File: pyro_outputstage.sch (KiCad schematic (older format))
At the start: 7 parts, among them Q302 BC847BDW1, U301 SI7232DN

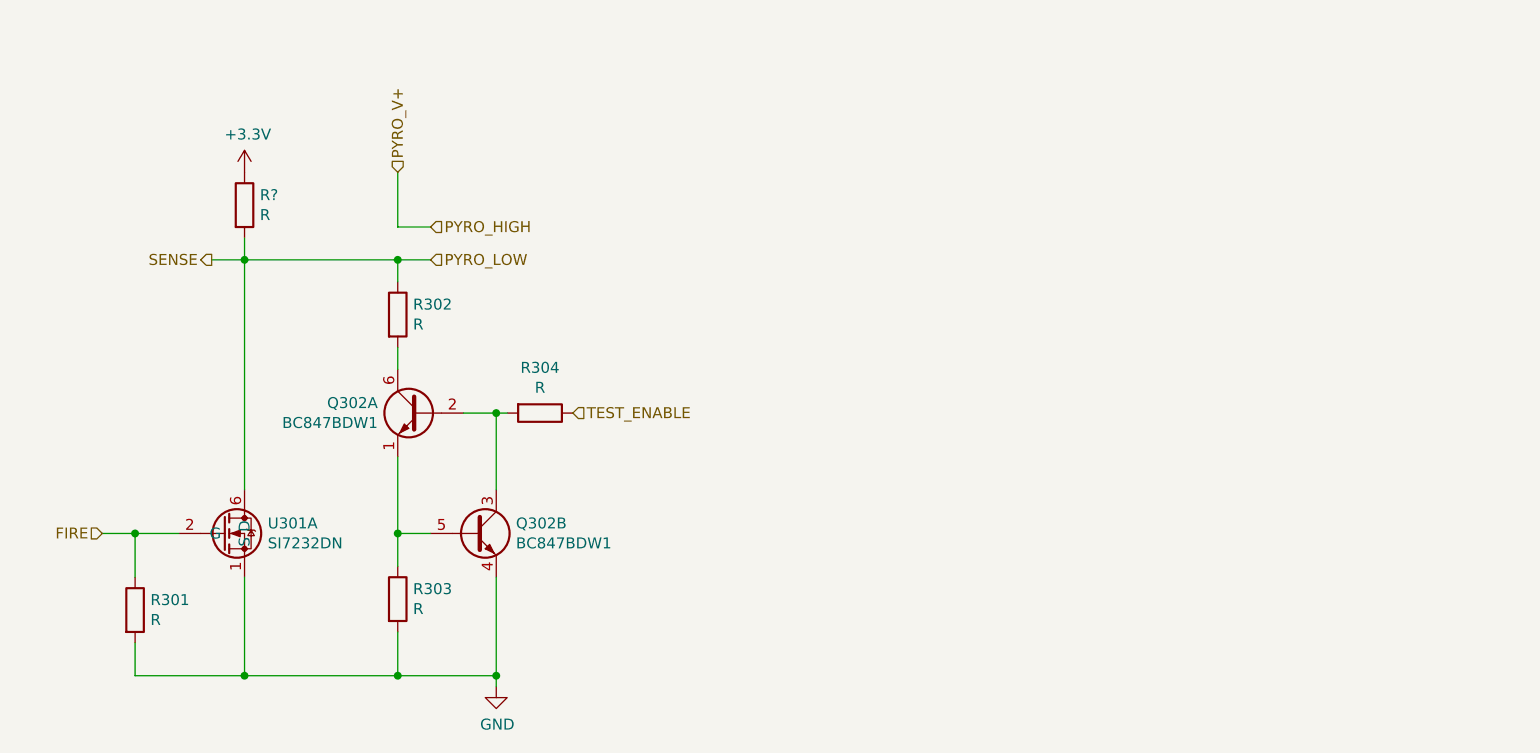
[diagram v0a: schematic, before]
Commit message: update pyro output stage. add a fuse to the test circuit and remove pullup for sense line
Signed-off-by: Thomas Schmid <tom@binary-kitchen.de>
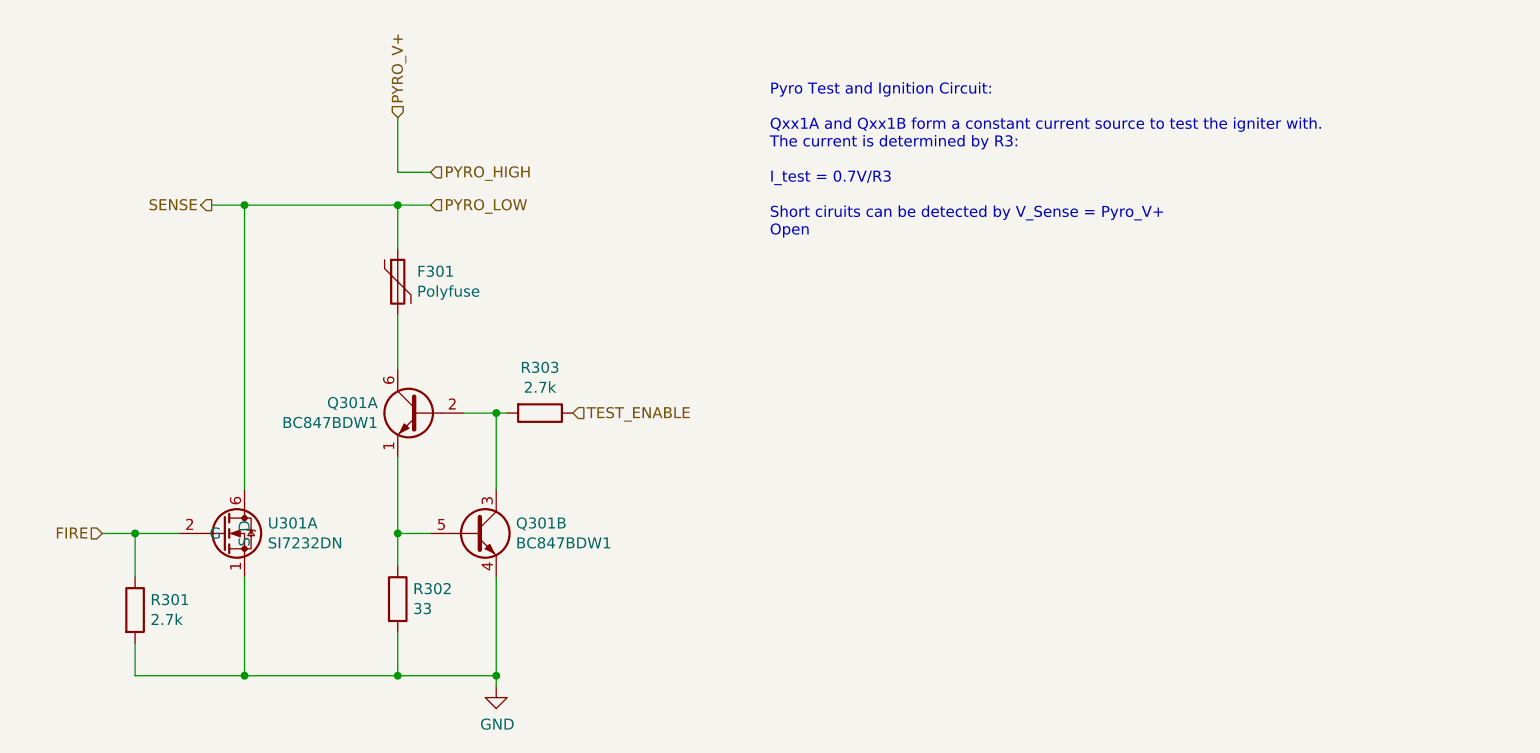
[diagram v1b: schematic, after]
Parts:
- removed R302, R?: R, Resistor_SMD:R_0603_1608Metric_Pad1.05x0.95mm_HandSolder, symbol Device:R
- added F301: Polyfuse, Fuse:Fuse_0603_1608Metric_Pad1.05x0.95mm_HandSolder, symbol Device:Polyfuse
- R301: value R -> 2.7k; footprint Resistor_SMD:R_0603_1608Metric_Pad1.05x0.95mm_HandSolder -> Resistor_SMD:R_0402_1005Metric
- R302: renamed from R303; value R -> 33; footprint Resistor_SMD:R_0603_1608Metric_Pad1.05x0.95mm_HandSolder -> Resistor_SMD:R_0402_1005Metric
- R303: renamed from R304; value R -> 2.7k; footprint Resistor_SMD:R_0603_1608Metric_Pad1.05x0.95mm_HandSolder -> Resistor_SMD:R_0402_1005Metric
- renumbered Q302 to Q301
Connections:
- net PYRO_LOW: now also F301.1
- net at Q301.6 (C1): now also F301.2
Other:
- note added: "Pyro Test and Ignition Circuit:\n\nQxx1A and Qxx1B form a constant current source to test the igniter with.\nThe current is determined by R3:\n\nI_test = 0.7V/R3\n\nShort ciruits can be detected by V_Sense = Pyro_V+\nOpen"
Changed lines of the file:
@@
 P 5850 4350
 AR Path="/5D4757F5" Ref="R?"  Part="1"
-AR Path="/5D473C9B/5D4757F5" Ref="R303"  Part="1"
+AR Path="/5D473C9B/5D4757F5" Ref="R302"  Part="1"
 AR Path="/5D47A891/5D4757F5" Ref="R?"  Part="1"
 AR Path="/5D47CE84/5D4757F5" Ref="R?"  Part="1"
-AR Path="/5D488E46/5D4757F5" Ref="R403"  Part="1"
-AR Path="/5D48B429/5D4757F5" Ref="R503"  Part="1"
-F 0 "R303" H 5920 4396 50  0000 L CNN
-F 1 "R" H 5920 4305 50  0000 L CNN
-F 2 "Resistor_SMD:R_0603_1608Metric_Pad1.05x0.95mm_HandSolder" V 5780 4350 50  0001 C CNN
+AR Path="/5D488E46/5D4757F5" Ref="R402"  Part="1"
+AR Path="/5D48B429/5D4757F5" Ref="R502"  Part="1"
+F 0 "R302" H 5920 4396 50  0000 L CNN
+F 1 "33" H 5920 4305 50  0000 L CNN
+F 2 "Resistor_SMD:R_0402_1005Metric" V 5780 4350 50  0001 C CNN
 F 3 "~" H 5850 4350 50  0001 C CNN
 	1    5850 4350
@@
 P 6300 4750
 AR Path="/5D475801" Ref="#PWR?"  Part="1"
-AR Path="/5D473C9B/5D475801" Ref="#PWR0136"  Part="1"
+AR Path="/5D473C9B/5D475801" Ref="#PWR0301"  Part="1"
 AR Path="/5D47A891/5D475801" Ref="#PWR?"  Part="1"
 AR Path="/5D47CE84/5D475801" Ref="#PWR?"  Part="1"
-AR Path="/5D488E46/5D475801" Ref="#PWR0137"  Part="1"
-AR Path="/5D48B429/5D475801" Ref="#PWR0138"  Part="1"
-F 0 "#PWR0136" H 6300 4500 50  0001 C CNN
+AR Path="/5D488E46/5D475801" Ref="#PWR0401"  Part="1"
+AR Path="/5D48B429/5D475801" Ref="#PWR0501"  Part="1"
+F 0 "#PWR0301" H 6300 4500 50  0001 C CNN
 F 1 "GND" H 6305 4577 50  0000 C CNN
 F 2 "" H 6300 4750 50  0001 C CNN
@@
 P 6500 3500
 AR Path="/5D47580C" Ref="R?"  Part="1"
-AR Path="/5D473C9B/5D47580C" Ref="R304"  Part="1"
+AR Path="/5D473C9B/5D47580C" Ref="R303"  Part="1"
 AR Path="/5D47A891/5D47580C" Ref="R?"  Part="1"
 AR Path="/5D47CE84/5D47580C" Ref="R?"  Part="1"
-AR Path="/5D488E46/5D47580C" Ref="R404"  Part="1"
-AR Path="/5D48B429/5D47580C" Ref="R504"  Part="1"
-F 0 "R304" V 6293 3500 50  0000 C CNN
-F 1 "R" V 6384 3500 50  0000 C CNN
-F 2 "Resistor_SMD:R_0603_1608Metric_Pad1.05x0.95mm_HandSolder" V 6430 3500 50  0001 C CNN
+AR Path="/5D488E46/5D47580C" Ref="R403"  Part="1"
+AR Path="/5D48B429/5D47580C" Ref="R503"  Part="1"
+F 0 "R303" V 6293 3500 50  0000 C CNN
+F 1 "2.7k" V 6384 3500 50  0000 C CNN
+F 2 "Resistor_SMD:R_0402_1005Metric" V 6430 3500 50  0001 C CNN
 F 3 "~" H 6500 3500 50  0001 C CNN
 	1    6500 3500
@@
 	6300 3500 6350 3500
 Connection ~ 6300 3500
-$Comp
-L Device:R R?
-U 1 1 5D475815
-P 5850 3050
-AR Path="/5D475815" Ref="R?"  Part="1"
-AR Path="/5D473C9B/5D475815" Ref="R302"  Part="1"
-AR Path="/5D47A891/5D475815" Ref="R?"  Part="1"
-AR Path="/5D47CE84/5D475815" Ref="R?"  Part="1"
-AR Path="/5D488E46/5D475815" Ref="R402"  Part="1"
-AR Path="/5D48B429/5D475815" Ref="R502"  Part="1"
-F 0 "R302" H 5920 3096 50  0000 L CNN
-F 1 "R" H 5920 3005 50  0000 L CNN
-F 2 "Resistor_SMD:R_0603_1608Metric_Pad1.05x0.95mm_HandSolder" V 5780 3050 50  0001 C CNN
-F 3 "~" H 5850 3050 50  0001 C CNN
-	1    5850 3050
-	1    0    0    -1
-$EndComp
-Wire Wire Line
-	5850 3200 5850 3300
-Wire Wire Line
-	6000 2800 5850 2800
-Wire Wire Line
-	5850 2800 5850 2900
-Wire Wire Line
-	6000 2650 5850 2650
-Wire Wire Line
-	5850 2650 5850 2400
-Wire Wire Line
-	5850 2800 5150 2800
-Wire Wire Line
-	5150 2800 5150 3850
-Connection ~ 5850 2800
+Wire Wire Line
+	6000 2400 5850 2400
+Wire Wire Line
+	5850 2400 5850 2150
 Wire Wire Line
 	5850 4700 5150 4700
@@
 AR Path="/5D48B429/5D475828" Ref="R501"  Part="1"
 F 0 "R301" H 4720 4446 50  0000 L CNN
-F 1 "R" H 4720 4355 50  0000 L CNN
-F 2 "Resistor_SMD:R_0603_1608Metric_Pad1.05x0.95mm_HandSolder" V 4580 4400 50  0001 C CNN
+F 1 "2.7k" H 4720 4355 50  0000 L CNN
+F 2 "Resistor_SMD:R_0402_1005Metric" V 4580 4400 50  0001 C CNN
 F 3 "~" H 4650 4400 50  0001 C CNN
 	1    4650 4400
@@
 P 5950 3500
 AR Path="/5D475835" Ref="Q?"  Part="1"
-AR Path="/5D473C9B/5D475835" Ref="Q302"  Part="1"
+AR Path="/5D473C9B/5D475835" Ref="Q301"  Part="1"
 AR Path="/5D47A891/5D475835" Ref="Q?"  Part="1"
 AR Path="/5D47CE84/5D475835" Ref="Q?"  Part="1"
-AR Path="/5D488E46/5D475835" Ref="Q402"  Part="1"
-AR Path="/5D48B429/5D475835" Ref="Q502"  Part="1"
-F 0 "Q302" H 6141 3546 50  0000 L CNN
+AR Path="/5D488E46/5D475835" Ref="Q401"  Part="1"
+AR Path="/5D48B429/5D475835" Ref="Q501"  Part="1"
+F 0 "Q301" H 6141 3546 50  0000 L CNN
 F 1 "BC847BDW1" H 6141 3455 50  0000 L CNN
 F 2 "Package_TO_SOT_SMD:SOT-363_SC-70-6" H 6150 3600 50  0001 C CNN
@@
 P 6200 4050
 AR Path="/5D47583B" Ref="Q?"  Part="2"
-AR Path="/5D473C9B/5D47583B" Ref="Q302"  Part="2"
+AR Path="/5D473C9B/5D47583B" Ref="Q301"  Part="2"
 AR Path="/5D47A891/5D47583B" Ref="Q?"  Part="2"
 AR Path="/5D47CE84/5D47583B" Ref="Q?"  Part="2"
-AR Path="/5D488E46/5D47583B" Ref="Q402"  Part="2"
-AR Path="/5D48B429/5D47583B" Ref="Q502"  Part="2"
-F 0 "Q302" H 6390 4096 50  0000 L CNN
+AR Path="/5D488E46/5D47583B" Ref="Q401"  Part="2"
+AR Path="/5D48B429/5D47583B" Ref="Q501"  Part="2"
+F 0 "Q301" H 6390 4096 50  0000 L CNN
 F 1 "BC847BDW1" H 6390 4005 50  0000 L CNN
 F 2 "Package_TO_SOT_SMD:SOT-363_SC-70-6" H 6400 4150 50  0001 C CNN
@@
 Text HLabel 6650 3500 2    50   Input ~ 0
 TEST_ENABLE
-Text HLabel 6000 2800 2    50   Input ~ 0
+Text HLabel 6000 2550 2    50   Input ~ 0
 PYRO_LOW
-Text HLabel 6000 2650 2    50   Input ~ 0
+Text HLabel 6000 2400 2    50   Input ~ 0
 PYRO_HIGH
-Text HLabel 5850 2400 1    50   Input ~ 0
+Text HLabel 5850 2150 1    50   Input ~ 0
 PYRO_V+
 Text HLabel 4500 4050 0    50   Input ~ 0
 FIRE
-Text HLabel 5000 2800 0    50   Output ~ 0
+Text HLabel 5000 2550 0    50   Output ~ 0
 SENSE
-Wire Wire Line
-	5000 2800 5150 2800
-Connection ~ 5150 2800
 $Comp
 L altimeter:SI7232DN U301
@@
 	1    0    0    -1
 $EndComp
-$Comp
-L Device:R R?
-U 1 1 5D503484
-P 5150 2550
-AR Path="/5D503484" Ref="R?"  Part="1"
-AR Path="/5D473C9B/5D503484" Ref="R?"  Part="1"
-AR Path="/5D47A891/5D503484" Ref="R?"  Part="1"
-AR Path="/5D47CE84/5D503484" Ref="R?"  Part="1"
-AR Path="/5D488E46/5D503484" Ref="R?"  Part="1"
-AR Path="/5D48B429/5D503484" Ref="R?"  Part="1"
-F 0 "R?" H 5220 2596 50  0000 L CNN
-F 1 "R" H 5220 2505 50  0000 L CNN
-F 2 "Resistor_SMD:R_0603_1608Metric_Pad1.05x0.95mm_HandSolder" V 5080 2550 50  0001 C CNN
-F 3 "~" H 5150 2550 50  0001 C CNN
-	1    5150 2550
-	1    0    0    -1
-$EndComp
-Wire Wire Line
-	5150 2700 5150 2800
-$Comp
-L power:+3.3V #PWR?
-U 1 1 5D50478E
-P 5150 2400
-AR Path="/5D488E46/5D50478E" Ref="#PWR?"  Part="1"
-AR Path="/5D473C9B/5D50478E" Ref="#PWR?"  Part="1"
-F 0 "#PWR?" H 5150 2250 50  0001 C CNN
-F 1 "+3.3V" H 5165 2573 50  0000 C CNN
-F 2 "" H 5150 2400 50  0001 C CNN
-F 3 "" H 5150 2400 50  0001 C CNN
-	1    5150 2400
-	1    0    0    -1
-$EndComp
+Text Notes 7550 2700 0    50   ~ 0
+Pyro Test and Ignition Circuit:\n\nQxx1A and Qxx1B form a constant current source to test the igniter with.\nThe current is determined by R3:\n\nI_test = 0.7V/R3\n\nShort ciruits can be detected by V_Sense = Pyro_V+\nOpen
+Wire Wire Line
+	5000 2550 5150 2550
+Connection ~ 5850 2550
+Wire Wire Line
+	5850 2550 6000 2550
+Connection ~ 5150 2550
+Wire Wire Line
+	5150 2550 5850 2550
+$Comp
+L Device:Polyfuse F301
+U 1 1 5D6F3FF8
+P 5850 2900
+AR Path="/5D473C9B/5D6F3FF8" Ref="F301"  Part="1"
+AR Path="/5D488E46/5D6F3FF8" Ref="F401"  Part="1"
+AR Path="/5D48B429/5D6F3FF8" Ref="F501"  Part="1"
+F 0 "F301" H 5938 2946 50  0000 L CNN
+F 1 "Polyfuse" H 5938 2855 50  0000 L CNN
+F 2 "Fuse:Fuse_0603_1608Metric_Pad1.05x0.95mm_HandSolder" H 5900 2700 50  0001 L CNN
+F 3 "~" H 5850 2900 50  0001 C CNN
+	1    5850 2900
+	1    0    0    -1
+$EndComp
+Wire Wire Line
+	5150 2550 5150 3850
+Wire Wire Line
+	5850 2750 5850 2550
+Wire Wire Line
+	5850 3050 5850 3300
 $EndSCHEMATC

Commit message: more work on schematic and layout
Signed-off-by: Thomas Schmid <tom@lfence.de>
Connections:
- net FIRE: now also U301.4 (G); no longer U301.2 (G)
- net GND: now also U301.3 (S); no longer U301.1 (S)
- net PYRO_LOW: now also U301.5 (D); no longer U301.6 (D)
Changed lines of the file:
@@
 AR Path="/5D488E46/5D475801" Ref="#PWR0401"  Part="1"
 AR Path="/5D48B429/5D475801" Ref="#PWR0501"  Part="1"
-F 0 "#PWR0301" H 6300 4500 50  0001 C CNN
+F 0 "#PWR0501" H 6300 4500 50  0001 C CNN
 F 1 "GND" H 6305 4577 50  0000 C CNN
 F 2 "" H 6300 4750 50  0001 C CNN
@@
 $Comp
 L altimeter:SI7232DN U301
-U 1 1 5D4F79DE
+U 2 1 5D4F79DE
 P 5150 4050
-AR Path="/5D473C9B/5D4F79DE" Ref="U301"  Part="1"
-AR Path="/5D488E46/5D4F79DE" Ref="U301"  Part="2"
+AR Path="/5D473C9B/5D4F79DE" Ref="U301"  Part="2"
+AR Path="/5D488E46/5D4F79DE" Ref="U301"  Part="1"
 AR Path="/5D48B429/5D4F79DE" Ref="U501"  Part="1"
 F 0 "U301" H 5256 4096 50  0000 L CNN
@@
 F 2 "Package_SO:Vishay_PowerPAK_1212-8_Dual" H 5150 4050 50  0001 C CNN
 F 3 "" H 5150 4050 50  0001 C CNN
-	1    5150 4050
+	2    5150 4050
 	1    0    0    -1
 $EndComp

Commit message: update
Signed-off-by: Thomas Schmid <tom@lfence.de>
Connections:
- net FIRE: now also U301.2 (G); no longer U301.4 (G)
- net GND: now also U301.1 (S); no longer U301.3 (S)
- net PYRO_LOW: now also U301.6 (D); no longer U301.5 (D)
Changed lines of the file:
@@
 $Descr A4 11693 8268
 encoding utf-8
-Sheet 3 5
+Sheet 5 5
 Title ""
 Date ""
@@
 AR Path="/5D488E46/5D4757F5" Ref="R402"  Part="1"
 AR Path="/5D48B429/5D4757F5" Ref="R502"  Part="1"
-F 0 "R302" H 5920 4396 50  0000 L CNN
+F 0 "R502" H 5920 4396 50  0000 L CNN
 F 1 "33" H 5920 4305 50  0000 L CNN
 F 2 "Resistor_SMD:R_0402_1005Metric" V 5780 4350 50  0001 C CNN
@@
 AR Path="/5D488E46/5D47580C" Ref="R403"  Part="1"
 AR Path="/5D48B429/5D47580C" Ref="R503"  Part="1"
-F 0 "R303" V 6293 3500 50  0000 C CNN
+F 0 "R503" V 6293 3500 50  0000 C CNN
 F 1 "2.7k" V 6384 3500 50  0000 C CNN
 F 2 "Resistor_SMD:R_0402_1005Metric" V 6430 3500 50  0001 C CNN
@@
 AR Path="/5D488E46/5D475828" Ref="R401"  Part="1"
 AR Path="/5D48B429/5D475828" Ref="R501"  Part="1"
-F 0 "R301" H 4720 4446 50  0000 L CNN
+F 0 "R501" H 4720 4446 50  0000 L CNN
 F 1 "2.7k" H 4720 4355 50  0000 L CNN
 F 2 "Resistor_SMD:R_0402_1005Metric" V 4580 4400 50  0001 C CNN
@@
 AR Path="/5D488E46/5D475835" Ref="Q401"  Part="1"
 AR Path="/5D48B429/5D475835" Ref="Q501"  Part="1"
-F 0 "Q301" H 6141 3546 50  0000 L CNN
+F 0 "Q501" H 6141 3546 50  0000 L CNN
 F 1 "BC847BDW1" H 6141 3455 50  0000 L CNN
 F 2 "Package_TO_SOT_SMD:SOT-363_SC-70-6" H 6150 3600 50  0001 C CNN
@@
 AR Path="/5D488E46/5D47583B" Ref="Q401"  Part="2"
 AR Path="/5D48B429/5D47583B" Ref="Q501"  Part="2"
-F 0 "Q301" H 6390 4096 50  0000 L CNN
+F 0 "Q501" H 6390 4096 50  0000 L CNN
 F 1 "BC847BDW1" H 6390 4005 50  0000 L CNN
 F 2 "Package_TO_SOT_SMD:SOT-363_SC-70-6" H 6400 4150 50  0001 C CNN
@@
 $Comp
 L altimeter:SI7232DN U301
-U 2 1 5D4F79DE
+U 1 1 5D4F79DE
 P 5150 4050
 AR Path="/5D473C9B/5D4F79DE" Ref="U301"  Part="2"
 AR Path="/5D488E46/5D4F79DE" Ref="U301"  Part="1"
 AR Path="/5D48B429/5D4F79DE" Ref="U501"  Part="1"
-F 0 "U301" H 5256 4096 50  0000 L CNN
+F 0 "U501" H 5256 4096 50  0000 L CNN
 F 1 "SI7232DN" H 5256 4005 50  0000 L CNN
 F 2 "Package_SO:Vishay_PowerPAK_1212-8_Dual" H 5150 4050 50  0001 C CNN
 F 3 "" H 5150 4050 50  0001 C CNN
-	2    5150 4050
+	1    5150 4050
 	1    0    0    -1
 $EndComp
@@
 AR Path="/5D488E46/5D6F3FF8" Ref="F401"  Part="1"
 AR Path="/5D48B429/5D6F3FF8" Ref="F501"  Part="1"
-F 0 "F301" H 5938 2946 50  0000 L CNN
+F 0 "F501" H 5938 2946 50  0000 L CNN
 F 1 "Polyfuse" H 5938 2855 50  0000 L CNN
 F 2 "Fuse:Fuse_0603_1608Metric_Pad1.05x0.95mm_HandSolder" H 5900 2700 50  0001 L CNN

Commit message: update to schematic and layout
Signed-off-by: Thomas Schmid <tom@lfence.de>
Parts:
- added R3: 68k, Resistor_SMD:R_0402_1005Metric, symbol Device:R
- added R4: 220k, Resistor_SMD:R_0402_1005Metric, symbol Device:R
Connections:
- net GND: now also R3.2
- net PYRO_LOW: now also R4.1
- new net SENSE: R3.1, R4.2
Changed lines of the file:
@@
 $Descr A4 11693 8268
 encoding utf-8
-Sheet 5 5
+Sheet 6 6
 Title ""
 Date ""
@@
 AR Path="/5D488E46/5D4757F5" Ref="R402"  Part="1"
 AR Path="/5D48B429/5D4757F5" Ref="R502"  Part="1"
-F 0 "R502" H 5920 4396 50  0000 L CNN
+AR Path="/5D4E7D5B/5D4757F5" Ref="R12"  Part="1"
+F 0 "R12" H 5920 4396 50  0000 L CNN
 F 1 "33" H 5920 4305 50  0000 L CNN
 F 2 "Resistor_SMD:R_0402_1005Metric" V 5780 4350 50  0001 C CNN
@@
 AR Path="/5D488E46/5D475801" Ref="#PWR0401"  Part="1"
 AR Path="/5D48B429/5D475801" Ref="#PWR0501"  Part="1"
-F 0 "#PWR0501" H 6300 4500 50  0001 C CNN
+AR Path="/5D4E7D5B/5D475801" Ref="#PWR0136"  Part="1"
+F 0 "#PWR0136" H 6300 4500 50  0001 C CNN
 F 1 "GND" H 6305 4577 50  0000 C CNN
 F 2 "" H 6300 4750 50  0001 C CNN
@@
 AR Path="/5D488E46/5D47580C" Ref="R403"  Part="1"
 AR Path="/5D48B429/5D47580C" Ref="R503"  Part="1"
-F 0 "R503" V 6293 3500 50  0000 C CNN
+AR Path="/5D4E7D5B/5D47580C" Ref="R13"  Part="1"
+F 0 "R13" V 6293 3500 50  0000 C CNN
 F 1 "2.7k" V 6384 3500 50  0000 C CNN
 F 2 "Resistor_SMD:R_0402_1005Metric" V 6430 3500 50  0001 C CNN
@@
 AR Path="/5D488E46/5D475828" Ref="R401"  Part="1"
 AR Path="/5D48B429/5D475828" Ref="R501"  Part="1"
-F 0 "R501" H 4720 4446 50  0000 L CNN
+AR Path="/5D4E7D5B/5D475828" Ref="R10"  Part="1"
+F 0 "R10" H 4720 4446 50  0000 L CNN
 F 1 "2.7k" H 4720 4355 50  0000 L CNN
 F 2 "Resistor_SMD:R_0402_1005Metric" V 4580 4400 50  0001 C CNN
@@
 AR Path="/5D488E46/5D475835" Ref="Q401"  Part="1"
 AR Path="/5D48B429/5D475835" Ref="Q501"  Part="1"
-F 0 "Q501" H 6141 3546 50  0000 L CNN
+AR Path="/5D4E7D5B/5D475835" Ref="Q1"  Part="1"
+F 0 "Q1" H 6141 3546 50  0000 L CNN
 F 1 "BC847BDW1" H 6141 3455 50  0000 L CNN
 F 2 "Package_TO_SOT_SMD:SOT-363_SC-70-6" H 6150 3600 50  0001 C CNN
@@
 AR Path="/5D488E46/5D47583B" Ref="Q401"  Part="2"
 AR Path="/5D48B429/5D47583B" Ref="Q501"  Part="2"
-F 0 "Q501" H 6390 4096 50  0000 L CNN
+AR Path="/5D4E7D5B/5D47583B" Ref="Q1"  Part="2"
+F 0 "Q1" H 6390 4096 50  0000 L CNN
 F 1 "BC847BDW1" H 6390 4005 50  0000 L CNN
 F 2 "Package_TO_SOT_SMD:SOT-363_SC-70-6" H 6400 4150 50  0001 C CNN
@@
 Text HLabel 4500 4050 0    50   Input ~ 0
 FIRE
-Text HLabel 5000 2550 0    50   Output ~ 0
+Text HLabel 4450 2550 0    50   Output ~ 0
 SENSE
 $Comp
@@
 AR Path="/5D473C9B/5D4F79DE" Ref="U301"  Part="2"
 AR Path="/5D488E46/5D4F79DE" Ref="U301"  Part="1"
-AR Path="/5D48B429/5D4F79DE" Ref="U501"  Part="1"
+AR Path="/5D48B429/5D4F79DE" Ref="U501"  Part="2"
+AR Path="/5D4E7D5B/5D4F79DE" Ref="U501"  Part="1"
 F 0 "U501" H 5256 4096 50  0000 L CNN
 F 1 "SI7232DN" H 5256 4005 50  0000 L CNN
@@
 AR Path="/5D488E46/5D6F3FF8" Ref="F401"  Part="1"
 AR Path="/5D48B429/5D6F3FF8" Ref="F501"  Part="1"
-F 0 "F501" H 5938 2946 50  0000 L CNN
+AR Path="/5D4E7D5B/5D6F3FF8" Ref="F1"  Part="1"
+F 0 "F1" H 5938 2946 50  0000 L CNN
 F 1 "Polyfuse" H 5938 2855 50  0000 L CNN
 F 2 "Fuse:Fuse_0603_1608Metric_Pad1.05x0.95mm_HandSolder" H 5900 2700 50  0001 L CNN
@@
 Wire Wire Line
 	5850 3050 5850 3300
+$Comp
+L Device:R R?
+U 1 1 5D4D8D4C
+P 4550 2850
+AR Path="/5D4D8D4C" Ref="R?"  Part="1"
+AR Path="/5D473C9B/5D4D8D4C" Ref="R3"  Part="1"
+AR Path="/5D47A891/5D4D8D4C" Ref="R?"  Part="1"
+AR Path="/5D47CE84/5D4D8D4C" Ref="R?"  Part="1"
+AR Path="/5D488E46/5D4D8D4C" Ref="R5"  Part="1"
+AR Path="/5D48B429/5D4D8D4C" Ref="R7"  Part="1"
+AR Path="/5D4E7D5B/5D4D8D4C" Ref="R9"  Part="1"
+F 0 "R9" H 4620 2896 50  0000 L CNN
+F 1 "68k" H 4620 2805 50  0000 L CNN
+F 2 "Resistor_SMD:R_0402_1005Metric" V 4480 2850 50  0001 C CNN
+F 3 "~" H 4550 2850 50  0001 C CNN
+	1    4550 2850
+	1    0    0    -1
+$EndComp
+$Comp
+L Device:R R?
+U 1 1 5D4D933B
+P 4850 2550
+AR Path="/5D4D933B" Ref="R?"  Part="1"
+AR Path="/5D473C9B/5D4D933B" Ref="R4"  Part="1"
+AR Path="/5D47A891/5D4D933B" Ref="R?"  Part="1"
+AR Path="/5D47CE84/5D4D933B" Ref="R?"  Part="1"
+AR Path="/5D488E46/5D4D933B" Ref="R6"  Part="1"
+AR Path="/5D48B429/5D4D933B" Ref="R8"  Part="1"
+AR Path="/5D4E7D5B/5D4D933B" Ref="R11"  Part="1"
+F 0 "R11" H 4920 2596 50  0000 L CNN
+F 1 "220k" H 4920 2505 50  0000 L CNN
+F 2 "Resistor_SMD:R_0402_1005Metric" V 4780 2550 50  0001 C CNN
+F 3 "~" H 4850 2550 50  0001 C CNN
+	1    4850 2550
+	0    1    1    0
+$EndComp
+Wire Wire Line
+	4700 2550 4550 2550
+Wire Wire Line
+	4550 2550 4550 2700
+Wire Wire Line
+	4550 2550 4450 2550
+Connection ~ 4550 2550
+$Comp
+L power:GND #PWR?
+U 1 1 5D4DA823
+P 4550 3000
+AR Path="/5D4DA823" Ref="#PWR?"  Part="1"
+AR Path="/5D473C9B/5D4DA823" Ref="#PWR0133"  Part="1"
+AR Path="/5D47A891/5D4DA823" Ref="#PWR?"  Part="1"
+AR Path="/5D47CE84/5D4DA823" Ref="#PWR?"  Part="1"
+AR Path="/5D488E46/5D4DA823" Ref="#PWR0134"  Part="1"
+AR Path="/5D48B429/5D4DA823" Ref="#PWR0135"  Part="1"
+AR Path="/5D4E7D5B/5D4DA823" Ref="#PWR0137"  Part="1"
+F 0 "#PWR0137" H 4550 2750 50  0001 C CNN
+F 1 "GND" H 4555 2827 50  0000 C CNN
+F 2 "" H 4550 3000 50  0001 C CNN
+F 3 "" H 4550 3000 50  0001 C CNN
+	1    4550 3000
+	1    0    0    -1
+$EndComp
 $EndSCHEMATC
